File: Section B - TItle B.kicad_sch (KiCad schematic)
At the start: 18 parts, among them J5 JST_SHBM04B-SRSS-TB, J6 Conn_02x07_Odd_Even, J7 THD-20-R, J9 Micro_SD_Card_Det, SW1 Right angle Tact button, U3 74LVC1G07SE-7, U6 RT9742GGJ5

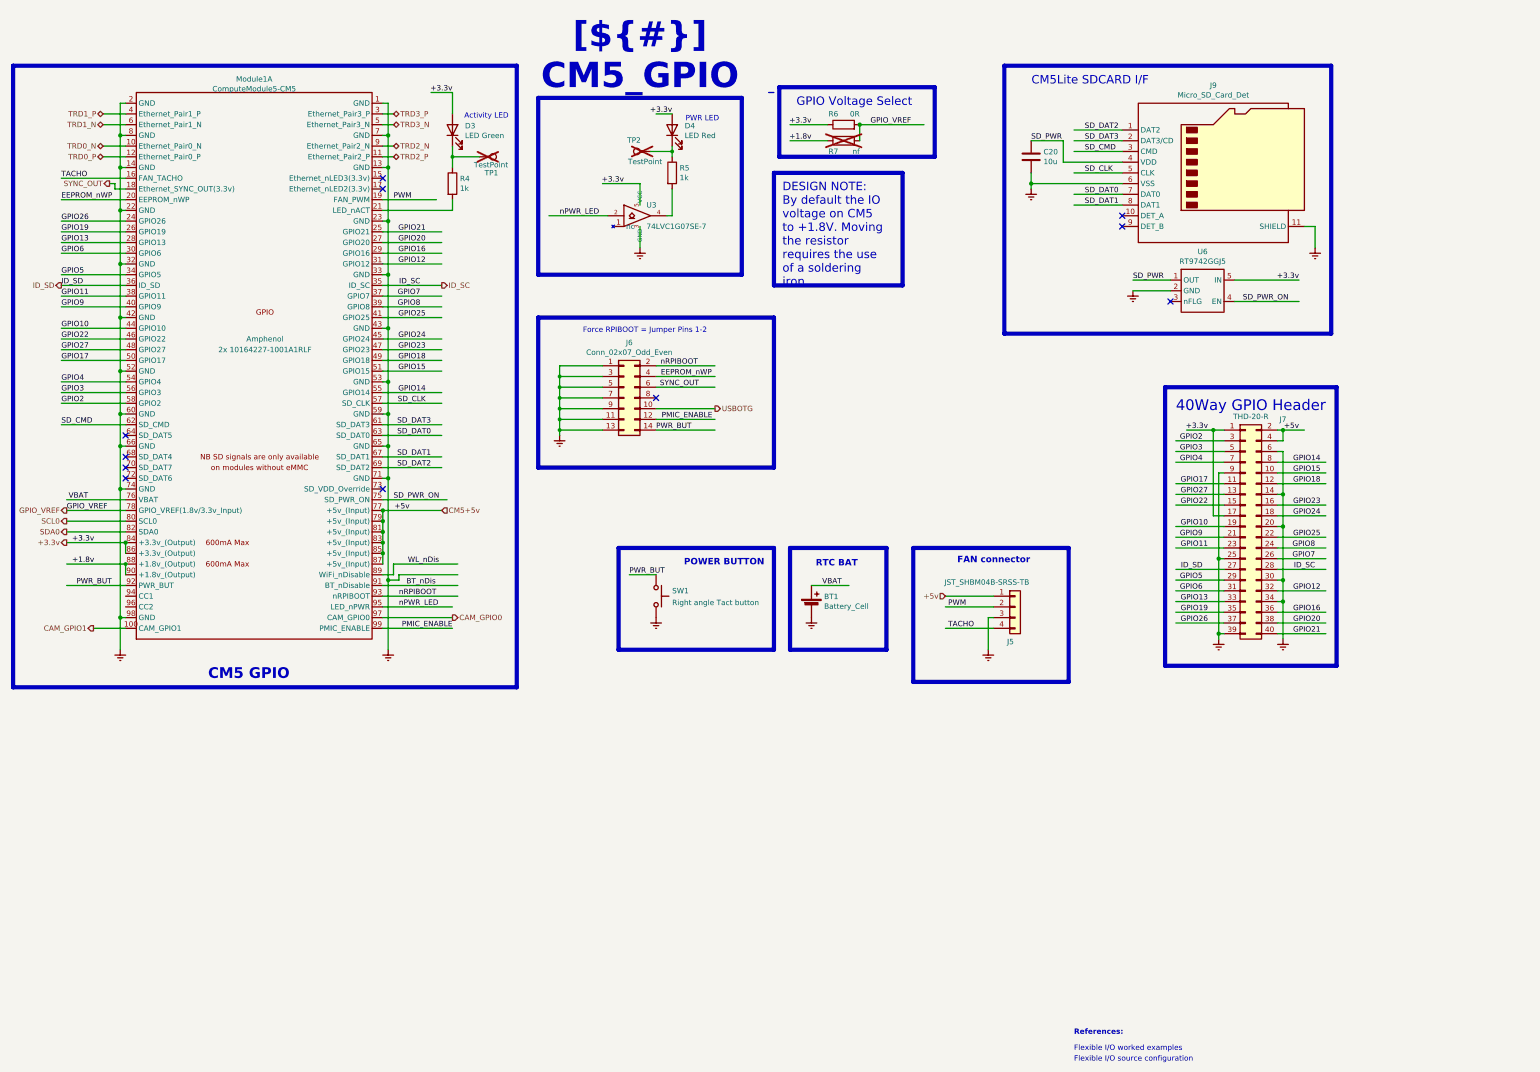
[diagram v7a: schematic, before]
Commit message: Removed Ethernet
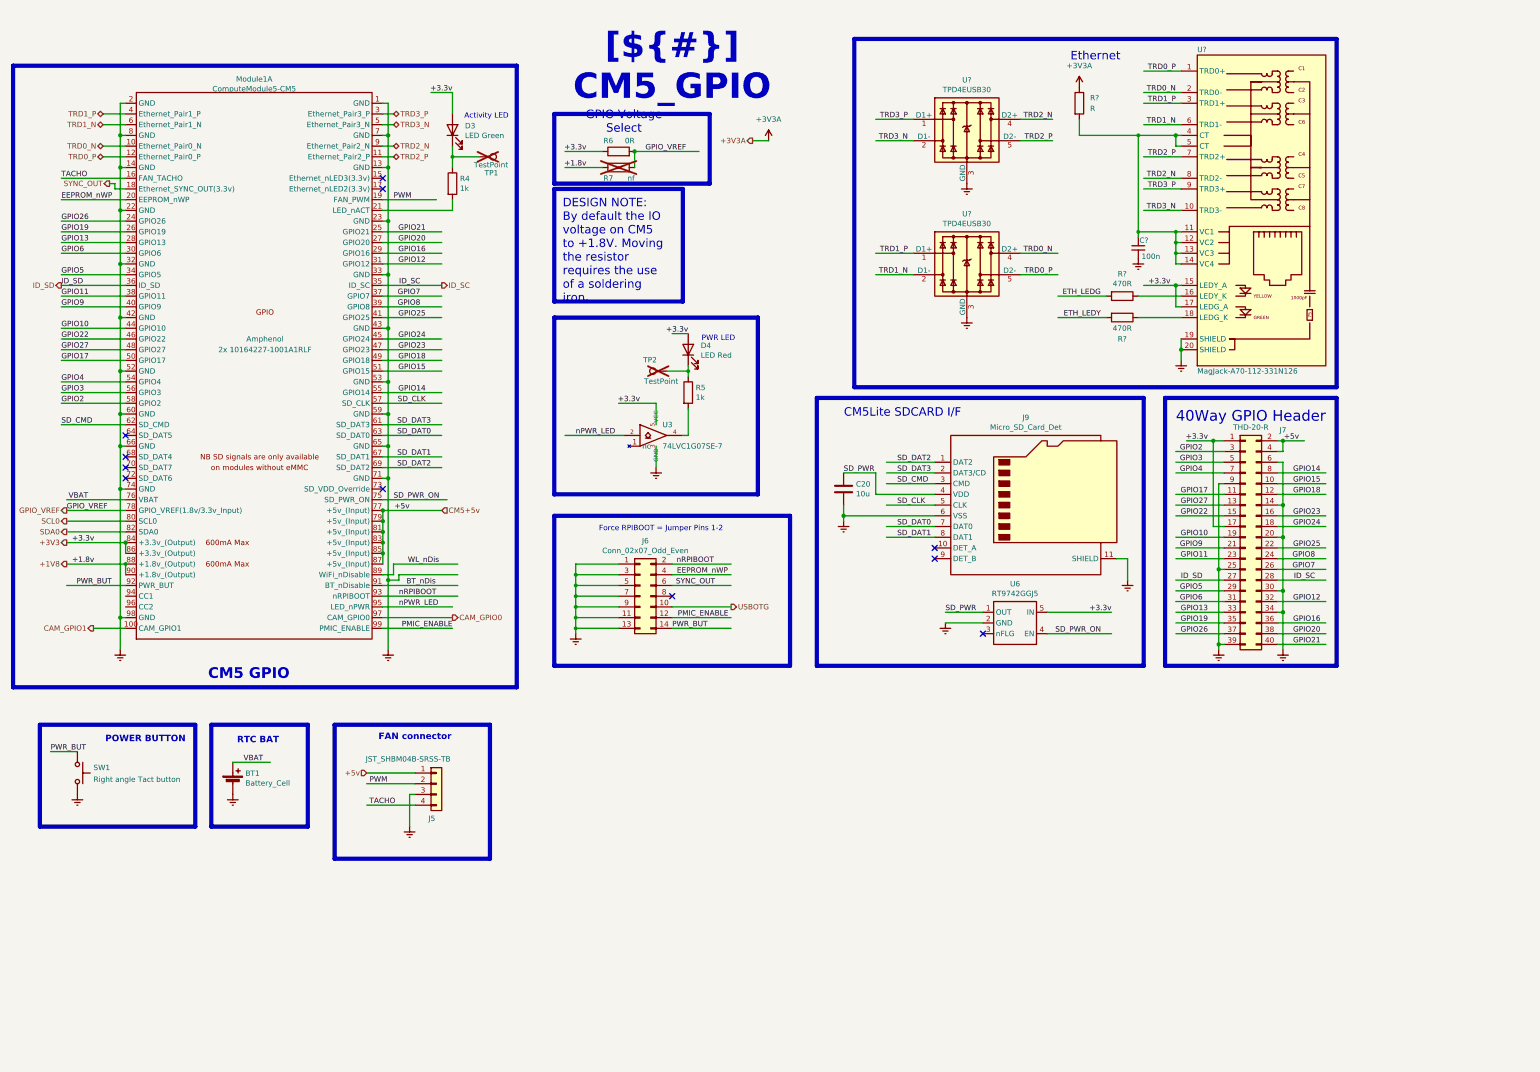
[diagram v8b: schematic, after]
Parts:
- added C?: 100n, symbol Device:C_Small
- added R?: R, symbol Device:R
- added R? (x2): 470R, Resistor_SMD:R_0402_1005Metric, symbol Device:R
- added U? (x2): TPD4EUSB30, Package_SON:USON-10_2.5x1.0mm_P0.5mm, symbol CM5IO:TPD4EUSB30
- added U?: MagJack-A70-112-331N126, CM5IO:TRJG0926HENL, symbol CM5IO:MagJack-A70-112-331N126
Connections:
- net TRD0_N: now also U?.2 (TRD0-), U?.4 (D2+), U?.7
- net TRD0_P: now also U?.1 (TRD0+), U?.5 (D2-), U?.6
- net TRD1_N: now also U?.2 (D1-), U?.6 (TRD1-), U?.9
- net TRD1_P: now also U?.1 (D1+), U?.10, U?.3 (TRD1+)
- net TRD2_N: now also U?.4 (D2+), U?.7, U?.8 (TRD2-)
- net TRD2_P: now also U?.5 (D2-), U?.6, U?.7 (TRD2+)
- net TRD3_N: now also U?.10 (TRD3-), U?.2 (D1-), U?.9
- net TRD3_P: now also U?.1 (D1+), U?.10, U?.9 (TRD3+)
- net +1.8v renamed +1V8
- net +3.3v renamed +3V3
- net +3V3: now also U?.15 (LEDY_A), U?.17 (LEDG_A)
- new net: U?.3 (GND), U?.8 (GND) (x2)
- new net: C?.1, R?.2, U?.11 (VC1), U?.12 (VC2), U?.13 (VC3), U?.14 (VC4), U?.4 (CT), U?.5 (CT)
- new net: R?.1, U?.16 (LEDY_K)
- new net: R?.1, U?.18 (LEDG_K)
- new net: U?.19 (SHIELD), U?.20 (SHIELD)
- new net +3V3A: R?.1
- new net ETH_LEDG: R?.2
- new net ETH_LEDY: R?.2
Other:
- note removed: "Flexible I/O source configuration"
- note removed: "Flexible I/O worked examples"
- note removed: "References:"
- moved on the sheet: BT1, C20, D4, J5, J6, J7, J9, R5, R6, R7, SW1, TP2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
